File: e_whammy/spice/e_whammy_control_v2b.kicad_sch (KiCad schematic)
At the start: 13 parts, among them U2 ${SIM.PARAMS}, U3 ${SIM.PARAMS}

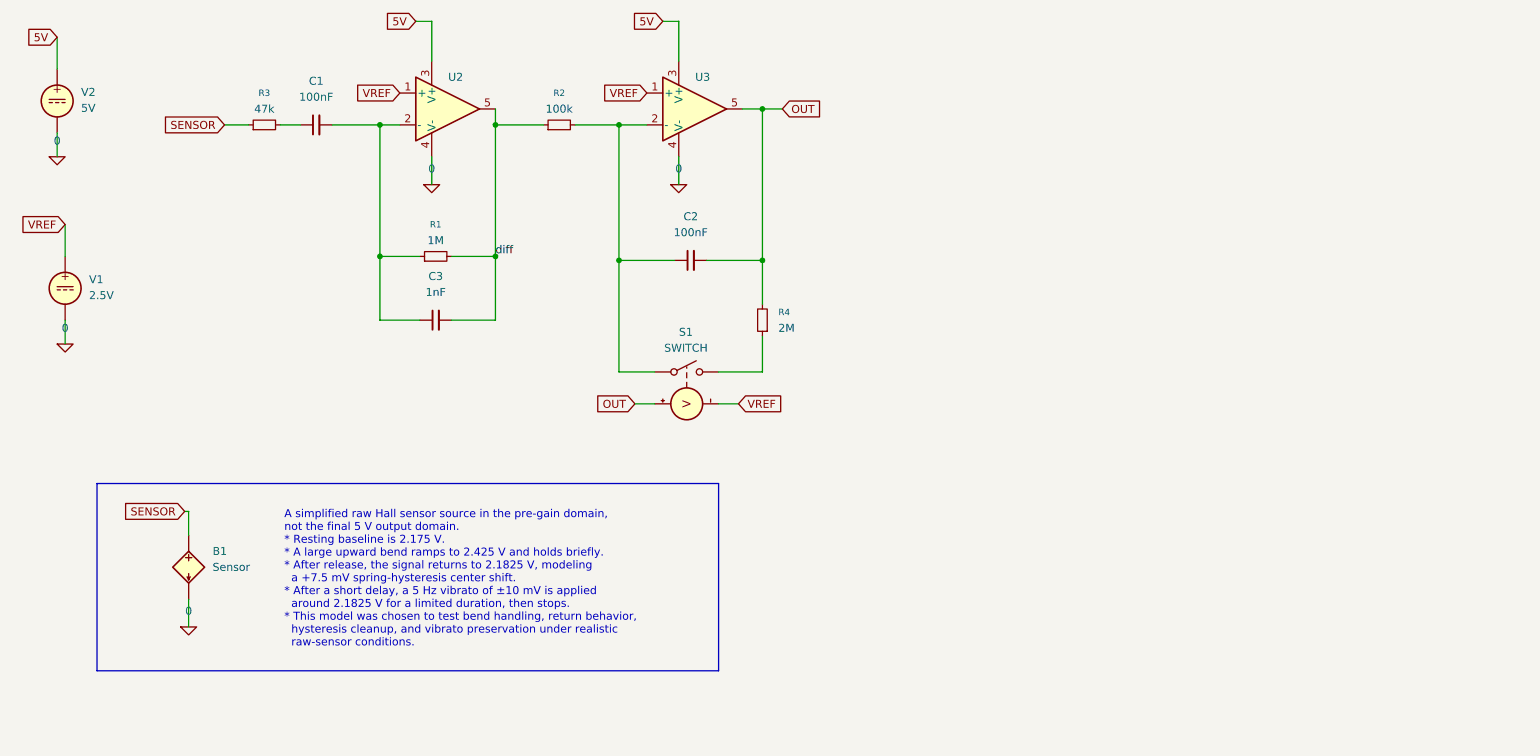
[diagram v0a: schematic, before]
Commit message: Added startup reset
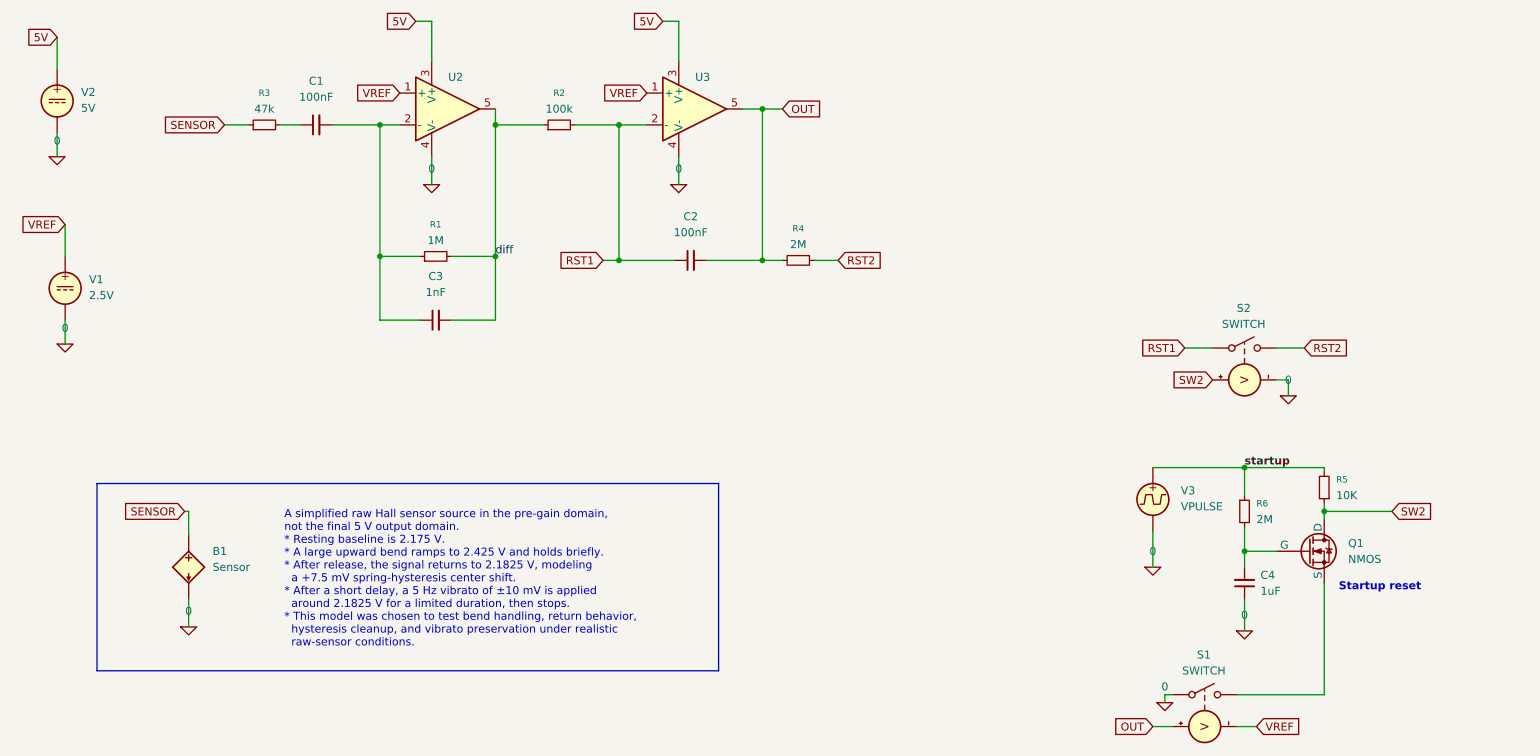
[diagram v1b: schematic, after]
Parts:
- added C4: 1uF, symbol Device:C_Small
- added Q1: NMOS, symbol Simulation_SPICE:NMOS
- added R5: 10K, symbol Device:R_Small
- added R6: 2M, symbol Device:R_Small
- added S2: SWITCH, symbol Simulation_SPICE:SWITCH
- added V3: VPULSE, symbol Simulation_SPICE:VPULSE
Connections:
- net 0: now also S1.1 (N+), C4.1, S2.4 (C-), V3.2
- net RST1: now reaches C2.1, R2.2, U3.2 (-)
- net RST1: now also S2.1 (N+); no longer S1.1 (N+)
- net at S1.2 (N-): now also Q1.3 (S); no longer R4.1
- new net: C4.2, Q1.2 (G), R6.2
- new net RST2: R4.1, S2.2 (N-)
- new net SW2: Q1.1 (D), R5.1, S2.3 (C+)
- new net startup: R5.2, R6.1, V3.1
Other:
- note added: "Startup reset"
- moved on the sheet: R4, S1

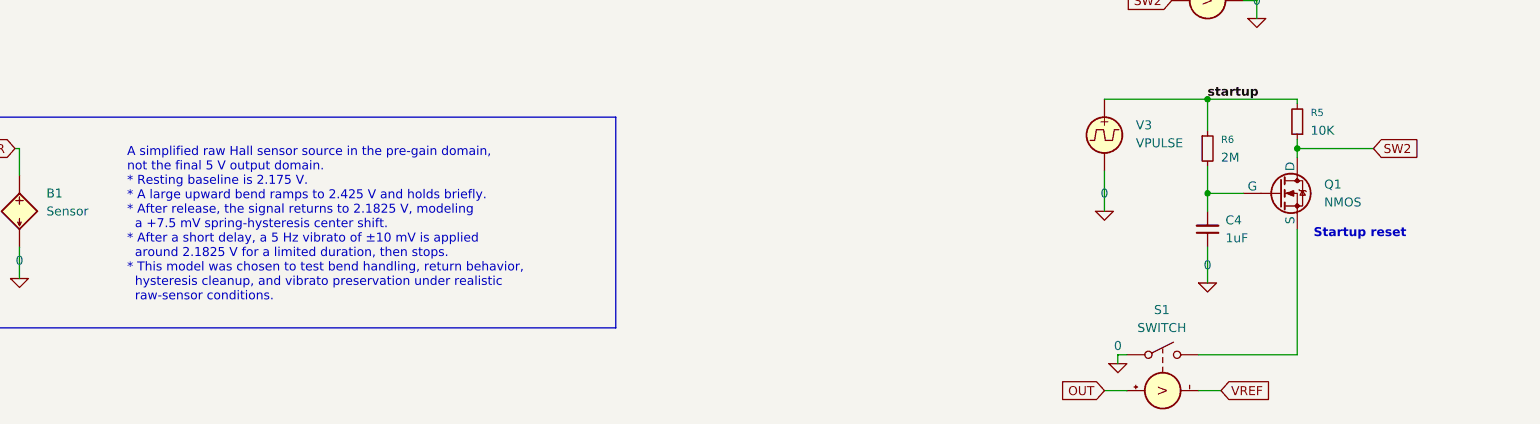
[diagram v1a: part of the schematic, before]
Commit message: Updated DC servo schematic for spice simulation
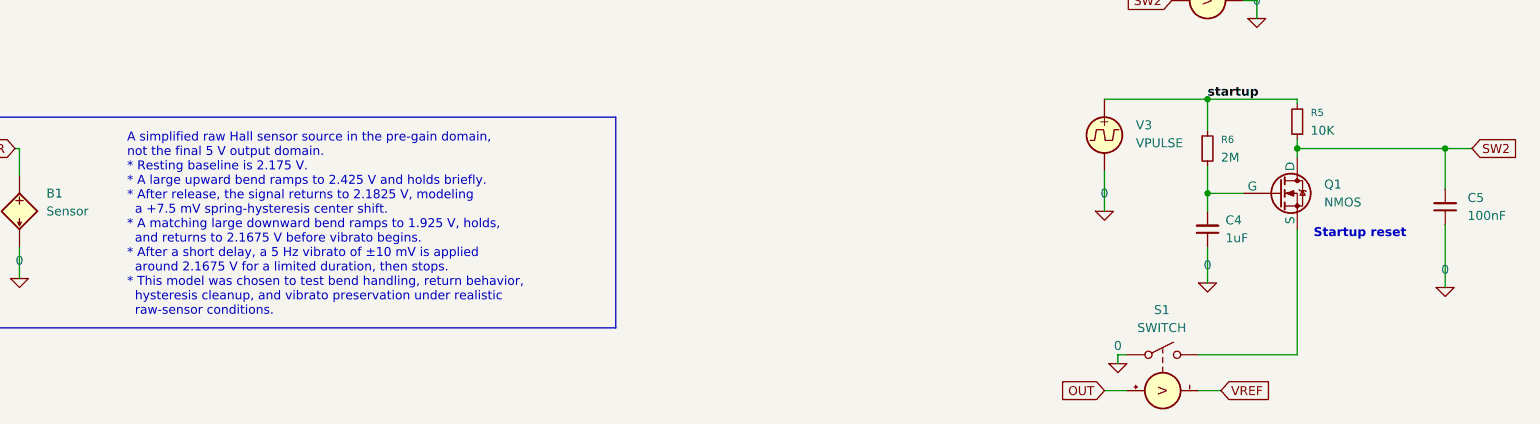
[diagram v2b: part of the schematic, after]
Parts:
- added C5: 100nF, symbol Device:C_Small
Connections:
- net 0: now also C5.1
- net SW2: now also C5.2
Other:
- note added: "A simplified raw Hall sensor source in the pre-gain domain, not the final 5 V output domain. * Resting baseline is 2.175 V. * A large upward bend ramps to 2.425 V and holds briefly. * After release, the signal returns to 2.1825 V, modeling a +7.5 mV spring-hysteresis center shift. * A matching large downward bend ramps to 1.925 V, holds, and returns to 2.1675 V before vibrato begins. * After a sh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"
- note removed: "A simplified raw Hall sensor source in the pre-gain domain, not the final 5 V output domain. * Resting baseline is 2.175 V. * A large upward bend ramps to 2.425 V and holds briefly. * After release, the signal returns to 2.1825 V, modeling a +7.5 mV spring-hysteresis center shift. * After a short delay, a 5 Hz vibrato of ±10 mV is applied around 2.1825 V for a limited duration, then stops. * This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"
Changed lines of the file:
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@@
 		)
 	)
-	(text "A simplified raw Hall sensor source in the pre-gain domain, \nnot the final 5 V output domain.\n* Resting baseline is 2.175 V.\n* A large upward bend ramps to 2.425 V and holds briefly.\n* After release, the signal returns to 2.1825 V, modeling \n  a +7.5 mV spring-hysteresis center shift.\n* After a short delay, a 5 Hz vibrato of ±10 mV is applied \n  around 2.1825 V for a limited duration, then stops.\n* This model was chosen to test bend handling, return behavior, \n  hysteresis cleanup, and vibrato preservation under realistic \n  raw-sensor conditions."
+	(text "A simplified raw Hall sensor source in the pre-gain domain, \nnot the final 5 V output domain.\n* Resting baseline is 2.175 V.\n* A large upward bend ramps to 2.425 V and holds briefly.\n* After release, the signal returns to 2.1825 V, modeling \n  a +7.5 mV spring-hysteresis center shift.\n* A matching large downward bend ramps to 1.925 V, holds, \n  and returns to 2.1675 V before vibrato begins.\n* After a short delay, a 5 Hz vibrato of ±10 mV is applied \n  around 2.1675 V for a limited duration, then stops.\n* This model was chosen to test bend handling, return behavior, \n  hysteresis cleanup, and vibrato preservation under realistic \n  raw-sensor conditions."
 		(exclude_from_sim no)
 		(at 75.565 127.635 0)
@@
 	)
 	(junction
+		(at 262.255 116.84)
+		(diameter 0)
+		(color 0 0 0 0)
+	)
+	(junction
 		(at 228.6 109.855)
 		(diameter 0)
@@
 	(wire
 		(pts
-			(xy 241.3 116.84) (xy 252.095 116.84)
+			(xy 241.3 116.84) (xy 262.255 116.84)
 		)
 		(stroke
@@
 	(wire
 		(pts
+			(xy 262.255 116.84) (xy 266.065 116.84)
+		)
+		(stroke
+			(width 0)
+			(type default)
+		)
+	)
+	(wire
+		(pts
 			(xy 219.075 90.805) (xy 223.52 90.805)
 		)
@@
 	(wire
 		(pts
+			(xy 262.255 127.635) (xy 262.255 136.525)
+		)
+		(stroke
+			(width 0)
+			(type default)
+		)
+	)
+	(wire
+		(pts
 			(xy 227.33 151.13) (xy 230.505 151.13)
 		)
@@
 		(pts
 			(xy 40.64 86.36) (xy 40.64 90.17)
+		)
+		(stroke
+			(width 0)
+			(type default)
+		)
+	)
+	(wire
+		(pts
+			(xy 262.255 116.84) (xy 262.255 122.555)
 		)
 		(stroke
@@
 	(global_label "SW2"
 		(shape input)
-		(at 252.095 116.84 0)
+		(at 266.065 116.84 0)
 		(fields_autoplaced yes)
 		(effects
@@
 		)
 		(property "Intersheetrefs" "${INTERSHEET_REFS}"
-			(at 258.9506 116.84 0)
+			(at 272.9206 116.84 0)
 			(effects
 				(font
@@
 			)
 		)
-		(property "Sim.Params" "type=\"B\" model=\"V=if(time<0.20,2.175*(time/0.20),if(time<0.35,2.175,if(time<0.45,2.175+(2.275-2.175)*(time-0.35)/0.10,if(time<0.55,2.275-(2.275-2.025)*(time-0.45)/0.10,if(time<0.65,2.025+(2.175-2.025)*(time-0.55)/0.10,if(time<2.00,2.175,if(time<2.25,2.175+(2.425-2.175)*(time-2.00)/0.25,if(time<3.00,2.425,if(time<3.25,2.425-((2.425-2.1825)*(time-3.00)/0.25),if(time<3.90,2.1825,if(time<4.90,2.1825+0.01*sin(2*pi*5*(time-3.90)),2.1825)))))))))))\""
+		(property "Sim.Params" "type=\"B\" model=\"V=if(time<0.20,2.175*(time/0.20),if(time<0.35,2.175,if(time<0.45,2.175+(2.275-2.175)*(time-0.35)/0.10,if(time<0.55,2.275-(2.275-2.025)*(time-0.45)/0.10,if(time<0.65,2.025+(2.175-2.025)*(time-0.55)/0.10,if(time<2.00,2.175,if(time<2.25,2.175+(2.425-2.175)*(time-2.00)/0.25,if(time<3.00,2.425,if(time<3.25,2.425-((2.425-2.1825)*(time-3.00)/0.25),if(time<3.50,2.1825,if(time<3.75,2.1825-((2.1825-1.925)*(time-3.50)/0.25),if(time<4.50,1.925,if(time<4.75,1.925+((2.1675-1.925)*(time-4.50)/0.25),if(time<5.40,2.1675,if(time<6.40,2.1675+0.01*sin(2*pi*5*(time-5.40)),2.1675)))))))))))))))\""
 			(at 64.135 128.2699 0)
 			(effects
@@
 	)
 	(symbol
+		(lib_id "Device:C_Small")
+		(at 262.255 125.095 180)
+		(unit 1)
+		(exclude_from_sim no)
+		(in_bom yes)
+		(on_board yes)
+		(dnp no)
+		(fields_autoplaced yes)
+		(property "Reference" "C5"
+			(at 265.43 123.8185 0)
+			(effects
+				(font
+					(size 1.27 1.27)
+				)
+				(justify right)
+			)
+		)
+		(property "Value" "100nF"
+			(at 265.43 126.3585 0)
+			(effects
+				(font
+					(size 1.27 1.27)
+				)
+				(justify right)
+			)
+		)
+		(property "Footprint" ""
+			(at 262.255 125.095 0)
+			(effects
+				(font
+					(size 1.27 1.27)
+				)
+				(hide yes)
+			)
+		)
+		(property "Datasheet" "~"
+			(at 262.255 125.095 0)
+			(effects
+				(font
+					(size 1.27 1.27)
+				)
+				(hide yes)
+			)
+		)
+		(property "Description" "Unpolarized capacitor, small symbol"
+			(at 262.255 125.095 0)
+			(effects
+				(font
+					(size 1.27 1.27)
+				)
+				(hide yes)
+			)
+		)
+		(pin "1"
+		)
+		(pin "2"
+		)
+		(instances
+			(project "e_whammy_control_v2b"
+				(path "/a157ea51-2828-471e-af10-4598cb486db8"
+					(reference "C5")
+					(unit 1)
+				)
+			)
+		)
+	)
+	(symbol
 		(lib_id "Simulation_SPICE:SWITCH")
 		(at 222.25 146.05 90)
@@
 					(unit 1)
 				)
+			)
+		)
+	)
+	(symbol
+		(lib_id "Simulation_SPICE:0")
+		(at 262.255 136.525 0)
+		(unit 1)
+		(exclude_from_sim no)
+		(in_bom yes)
+		(on_board yes)
+		(dnp no)
+		(fields_autoplaced yes)
+		(property "Reference" "#GND010"
+			(at 262.255 141.605 0)
+			(effects
+				(font
+					(size 1.27 1.27)
+				)
+				(hide yes)
+			)
+		)
+		(property "Value" "0"
+			(at 262.255 133.985 0)
+			(effects
+				(font
+					(size 1.27 1.27)
+				)
+			)
+		)
+		(property "Footprint" ""
+			(at 262.255 136.525 0)
+			(effects
+				(font
+					(size 1.27 1.27)
+				)
+				(hide yes)
+			)
+		)
+		(property "Datasheet" "https://ngspice.sourceforge.io/docs/ngspice-html-manual/manual.xhtml#subsec_Circuit_elements__device"
+			(at 262.255 146.685 0)
+			(effects
+				(font
+					(size 1.27 1.27)
+				)
+				(hide yes)
+			)
+		)
+		(property "Description" "0V reference potential for simulation"
+			(at 262.255 144.145 0)
+			(effects
+				(font
+					(size 1.27 1.27)
+				)
+				(hide yes)
+			)
+		)
+		(pin "1"
+		)
+		(instances
+			(project "e_whammy_control_v2b"
+				(path "/a157ea51-2828-471e-af10-4598cb486db8"
+					(reference "#GND010")
+					(unit 1)
+				)
